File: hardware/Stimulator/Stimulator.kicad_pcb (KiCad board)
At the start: 2 copper layers, 49.5 x 33 mm, 52 parts, among them P1 CONN_3X2, P10 CONN_10X2, P12 CONN_8X2, P2 CONN_9X2, Q1 2N7002, Q2 2N7002, Q3 2N7002, Q4 2N7002, Q5 2N7002, Q6 2N7002, U1 MCP42010, U2 MCP42010, U3 MCP42010, U4 MCP42010

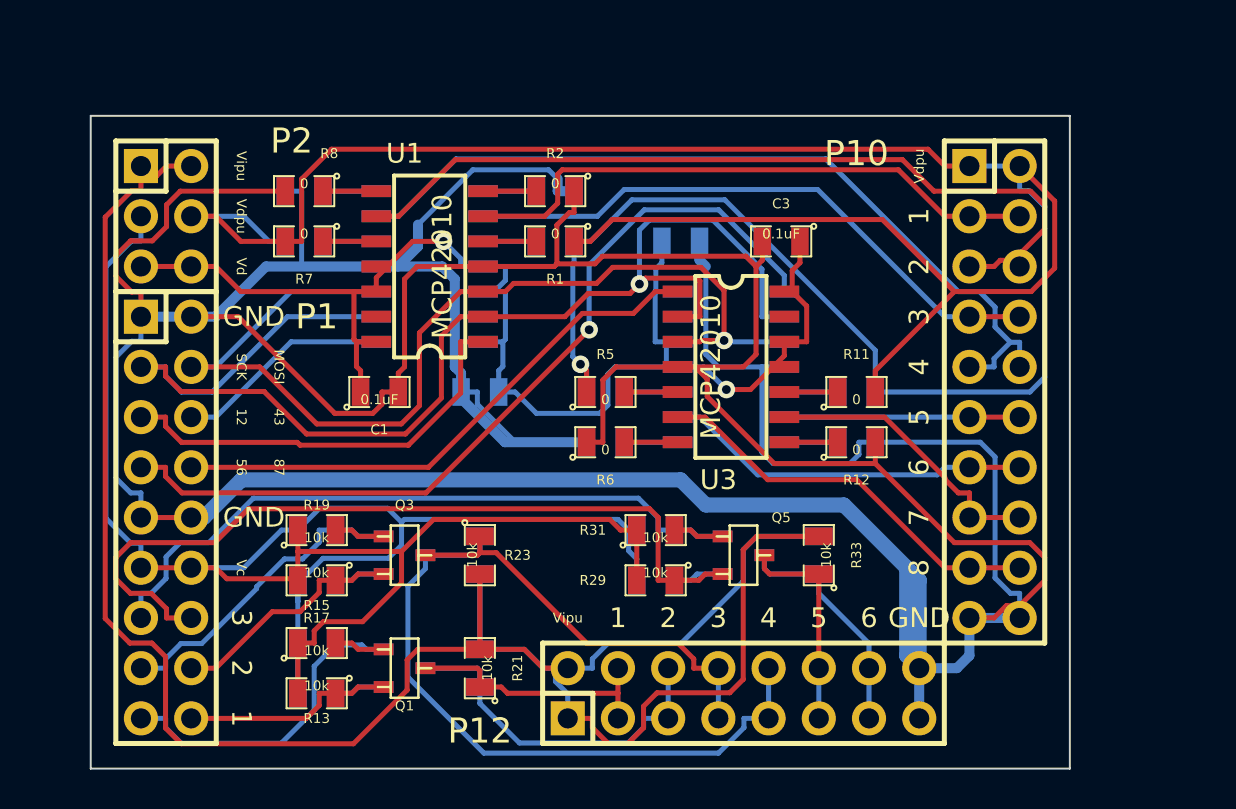
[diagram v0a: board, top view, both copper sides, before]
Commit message: 
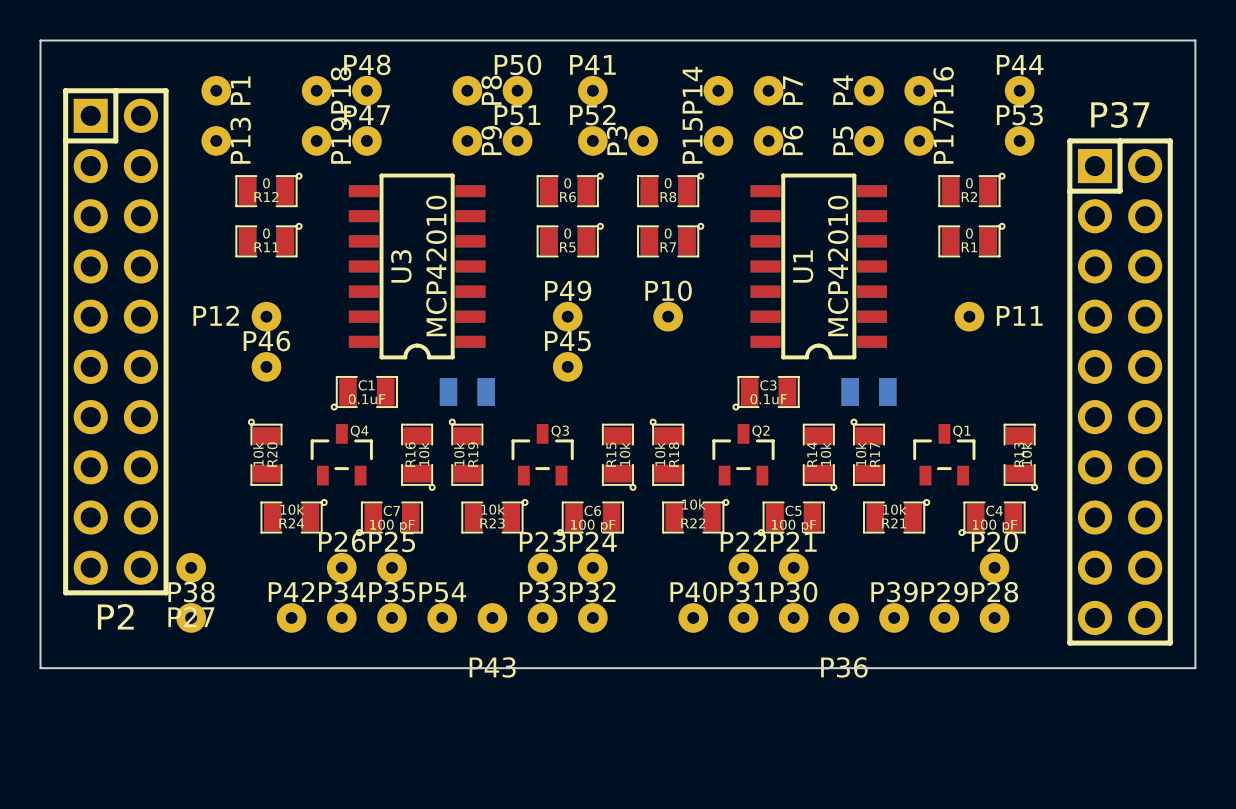
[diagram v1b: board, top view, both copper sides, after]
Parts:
- removed Q5, Q6: 2N7002, Transistors_SMD:sot23
- removed R29, R30, R31, R32, R33, R34: 10k, SMD_Packages:SM0805
- added C5: 100 pF, SMD_Packages:SM0805, F.Cu at (160.0, 82.5)
- added C6: 100 pF, SMD_Packages:SM0805, F.Cu at (149.9, 82.5)
- added C7: 100 pF, SMD_Packages:SM0805, F.Cu at (139.7, 82.5)
- added C8: 0.1uF, SMD_Packages:SM0805, B.Cu at (143.5, 76.2)
- added P11: CONN_1, Stimulator:1PIN, F.Cu at (168.9, 72.4)
- added P13: CONN_1, Stimulator:1PIN, F.Cu at (130.8, 63.5)
- added P14: CONN_1, Stimulator:1PIN, F.Cu at (156.2, 61.0)
- added P15: CONN_1, Stimulator:1PIN, F.Cu at (156.2, 63.5)
- added P16: CONN_1, Stimulator:1PIN, F.Cu at (166.4, 61.0)
- added P17: CONN_1, Stimulator:1PIN, F.Cu at (166.4, 63.5)
- added P18: CONN_1, Stimulator:1PIN, F.Cu at (135.9, 61.0)
- added P19: CONN_1, Stimulator:1PIN, F.Cu at (135.9, 63.5)
- added P20: CONN_1, Stimulator:1PIN, F.Cu at (170.2, 85.1)
- added P21: CONN_1, Stimulator:1PIN, F.Cu at (160.0, 85.1)
- added P22: CONN_1, Stimulator:1PIN, F.Cu at (157.5, 85.1)
- added P23: CONN_1, Stimulator:1PIN, F.Cu at (147.3, 85.1)
- added P24: CONN_1, Stimulator:1PIN, F.Cu at (149.9, 85.1)
- added P25: CONN_1, Stimulator:1PIN, F.Cu at (139.7, 85.1)
- added P26: CONN_1, Stimulator:1PIN, F.Cu at (137.2, 85.1)
- added P27: CONN_1, Stimulator:1PIN, F.Cu at (129.5, 85.1)
- added P28: CONN_1, Stimulator:1PIN, F.Cu at (170.2, 87.6)
- added P29: CONN_1, Stimulator:1PIN, F.Cu at (167.6, 87.6)
- added P3: CONN_1, Stimulator:1PIN, F.Cu at (152.4, 63.5)
- added P30: CONN_1, Stimulator:1PIN, F.Cu at (160.0, 87.6)
- added P31: CONN_1, Stimulator:1PIN, F.Cu at (157.5, 87.6)
- added P32: CONN_1, Stimulator:1PIN, F.Cu at (149.9, 87.6)
- added P33: CONN_1, Stimulator:1PIN, F.Cu at (147.3, 87.6)
- added P34: CONN_1, Stimulator:1PIN, F.Cu at (137.2, 87.6)
- added P35: CONN_1, Stimulator:1PIN, F.Cu at (139.7, 87.6)
- added P36: CONN_1, Stimulator:1PIN, F.Cu at (162.6, 87.6)
- added P37: CONN_10X2, Pin_Headers:Pin_Header_Straight_2x10, F.Cu at (176.5, 76.2)
- added P38: CONN_1, Stimulator:1PIN, F.Cu at (129.5, 87.6)
- added P39: CONN_1, Stimulator:1PIN, F.Cu at (165.1, 87.6)
- added P4: CONN_1, Stimulator:1PIN, F.Cu at (163.8, 61.0)
- added P40: CONN_1, Stimulator:1PIN, F.Cu at (154.9, 87.6)
- added P41: CONN_1, Stimulator:1PIN, F.Cu at (149.9, 61.0)
- added P42: CONN_1, Stimulator:1PIN, F.Cu at (134.6, 87.6)
- added P43: CONN_1, Stimulator:1PIN, F.Cu at (144.8, 87.6)
- added P44: CONN_1, Stimulator:1PIN, F.Cu at (171.4, 61.0)
- added P45: CONN_1, Stimulator:1PIN, F.Cu at (148.6, 74.9)
- added P46: CONN_1, Stimulator:1PIN, F.Cu at (133.3, 74.9)
- added P47: CONN_1, Stimulator:1PIN, F.Cu at (138.4, 63.5)
- added P48: CONN_1, Stimulator:1PIN, F.Cu at (138.4, 61.0)
- added P49: CONN_1, Stimulator:1PIN, F.Cu at (148.6, 72.4)
- added P5: CONN_1, Stimulator:1PIN, F.Cu at (163.8, 63.5)
- added P50: CONN_1, Stimulator:1PIN, F.Cu at (146.1, 61.0)
- added P51: CONN_1, Stimulator:1PIN, F.Cu at (146.1, 63.5)
- added P52: CONN_1, Stimulator:1PIN, F.Cu at (149.9, 63.5)
- added P53: CONN_1, Stimulator:1PIN, F.Cu at (171.4, 63.5)
- added P54: CONN_1, Stimulator:1PIN, F.Cu at (142.2, 87.6)
- added P6: CONN_1, Stimulator:1PIN, F.Cu at (158.8, 63.5)
- added P7: CONN_1, Stimulator:1PIN, F.Cu at (158.8, 61.0)
- added P8: CONN_1, Stimulator:1PIN, F.Cu at (143.5, 61.0)
- added P9: CONN_1, Stimulator:1PIN, F.Cu at (143.5, 63.5)
- C4: value 0.1uF -> 100 pF; moved to F.Cu
- P1: value CONN_3X2 -> CONN_1; footprint Pin_Headers:Pin_Header_Straight_2x03 -> Stimulator:1PIN
- P10: value CONN_10X2 -> CONN_1; footprint Pin_Headers:Pin_Header_Straight_2x10 -> Stimulator:1PIN
- P12: value CONN_8X2 -> CONN_1; footprint Pin_Headers:Pin_Header_Straight_2x08 -> Stimulator:1PIN
- P2: value CONN_9X2 -> CONN_10X2; footprint Pin_Headers:Pin_Header_Straight_2x09 -> Pin_Headers:Pin_Header_Straight_2x10
- Q2, Q4, R14, R16, R18, R20, R22, R24: moved to F.Cu
- moved R13 37.6 mm to (171.4, 79.4), turned to 90 degrees
- moved R12 32.4 mm to (133.3, 66.0), turned to 180 degrees
- moved R26 32.4 mm to (133.3, 66.0), turned to 0 degrees
- moved R11 30.8 mm to (133.3, 68.6), turned to 180 degrees
- moved R25 30.8 mm to (133.3, 68.6), turned to 0 degrees
- moved P12 30.7 mm to (133.3, 72.4)
- moved R17 29.5 mm to (163.8, 79.4), turned to 270 degrees
- moved Q1 29.4 mm to (167.6, 79.4), turned to 0 degrees
- moved R14 27.1 mm to (161.3, 79.4), turned to 90 degrees
- moved R21 22.3 mm to (165.1, 82.5), turned to 180 degrees
- moved R18 21.5 mm to (153.7, 79.4), turned to 270 degrees
- moved C4 21.1 mm to (170.2, 82.5)
- moved R1 21.0 mm to (168.9, 68.6)
- moved R10 21.0 mm to (168.9, 66.0)
- moved R2 21.0 mm to (168.9, 66.0)
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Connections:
- C4 pad 1: /Vd -> /EIN_1
- C4 pad 2: GND -> /IN_1
- P1 pad 1: /Vipu -> GND
- P10 pad 1: /Vdpu -> Net-(P10-Pad1)
- P12 pad 1: /Vipu -> Net-(P12-Pad1)
- P2 pad 10: GND -> Net-(P2-Pad10)
- P2 pad 11: /Vc -> Net-(P2-Pad11)
- P2 pad 12: /Vc -> Net-(P2-Pad12)
- P2 pad 13: /IN_6 -> Net-(P2-Pad13)
- P2 pad 14: /IN_5 -> Net-(P2-Pad14)
- P2 pad 15: /IN_4 -> Net-(P2-Pad15)
- P2 pad 16: /IN_3 -> Net-(P2-Pad16)
- P2 pad 17: /IN_2 -> Net-(P2-Pad17)
- P2 pad 18: /IN_1 -> Net-(P2-Pad18)
- P2 pad 2: GND -> Net-(P2-Pad2)
- P2 pad 3: /SCK -> Net-(P2-Pad3)
- P2 pad 4: /MOSI -> Net-(P2-Pad4)
- P2 pad 5: /CS_12 -> Net-(P2-Pad5)
- P2 pad 6: /CS_43 -> Net-(P2-Pad6)
- P2 pad 7: /CS_56 -> Net-(P2-Pad7)
- P2 pad 8: /CS_87 -> Net-(P2-Pad8)
- P2 pad 9: GND -> Net-(P2-Pad9)
- R1 pad 1: /Vdpu -> /Vdpu_14
- R11 pad 2: /Vdpu -> /Vdpu_58
- R21 pad 2: /Vipu -> /Vipu12
- R22 pad 2: /Vipu -> /Vipu12
- R23 pad 2: /Vipu -> /Vipu34
- R24 pad 2: /Vipu -> /Vipu34
- R25 pad 1: /Vdpu -> /Vdpu_58
- R27 pad 2: /Vdpu -> /Vdpu_58
- R3 pad 1: /Vdpu -> /Vdpu_14
- R5 pad 1: /Vdpu -> /Vdpu_58
- R7 pad 2: /Vdpu -> /Vdpu_14
- R9 pad 2: /Vdpu -> /Vdpu_14
- U1 pad 13: (no net) -> Net-(P10-Pad1)
- U2 pad 13: (no net) -> Net-(P11-Pad1)
- U2 pad 6: /OUT4 -> /OUT3
- U2 pad 9: /OUT3 -> /OUT4
- U3 pad 1: /CS_87 -> /CS_56
- U3 pad 13: (no net) -> Net-(P12-Pad1)
- U3 pad 6: /OUT8 -> /OUT5
- U3 pad 9: /OUT7 -> /OUT6
- U4 pad 1: /CS_56 -> /CS_78
- U4 pad 13: (no net) -> Net-(P49-Pad1)
- U4 pad 6: /OUT5 -> /OUT7
- U4 pad 9: /OUT6 -> /OUT8
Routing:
- net GND: track 281.5 -> 0.00 mm
- net /Vdpu: track 142.5 -> 0.00 mm, vias 1 -> 0
- net /Vipu: track 112.3 -> 0.00 mm
- net /Vc: track 103.0 -> 0.00 mm
- net /Vd: track 71.9 -> 0.00 mm, vias 2 -> 0
- net /SCK: track 66.0 -> 0.00 mm, vias 1 -> 0
- net /MOSI: track 53.0 -> 0.00 mm, vias 1 -> 0
- net /CS_56: track 43.4 -> 0.00 mm, vias 1 -> 0
- net /OUT4: track 42.3 -> 0.00 mm
- net /OUT2: track 42.2 -> 0.00 mm
- net /IN_5: track 41.2 -> 0.00 mm
- net /IN_6: track 34.5 -> 0.00 mm
- net /EIN_4: track 33.5 -> 0.00 mm
- net /OUT3: track 30.4 -> 0.00 mm
- net /OUT1: track 30.0 -> 0.00 mm
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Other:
- board size 49.5 x 33 mm -> 58.4 x 31.8 mm
- board text removed: "1"
- board text removed: "12"
- board text removed: "2"
- board text removed: "3"
- board text removed: "4"
- board text removed: "43"
- board text removed: "5"
- board text removed: "56"
- board text removed: "6"
- board text removed: "7"
- board text removed: "8"
- board text removed: "87"
- board text removed: "GND"
- board text removed: "MOSI"
- board text removed: "SCK"
- board text removed: "Vc"
- board text removed: "Vd"
- board text removed: "Vdpu"
- board text removed: "Vipu"

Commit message: 
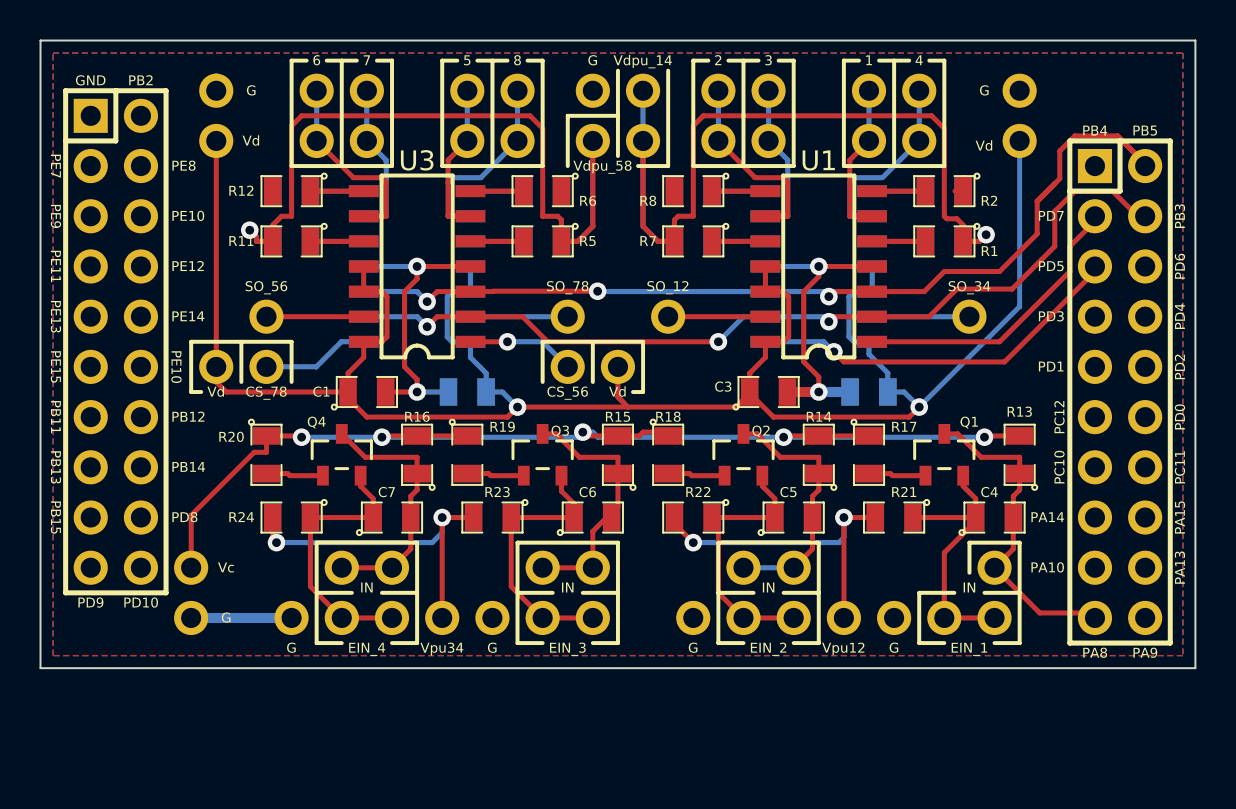
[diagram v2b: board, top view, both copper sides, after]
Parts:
- added P55: CONN_1, Stimulator:1PIN_A, F.Cu at (151.1, 74.9)
- added P56: CONN_1, Stimulator:1PIN_A, F.Cu at (130.8, 74.9)
- added P57: CONN_1, Stimulator:1PIN_A, F.Cu at (152.4, 61.0)
- P1, P10, P11, P12, P13, P14, P15, P16, P17, P18, P19, P20, P21, P22, P23, P24, P25, P26, P27, P28, P29, P3, P30, P31, P32, P33, P34, P35, P36, P38, P39, P4, P40, P41, P42, P43, P44, P45, P46, P47, P48, P49, P5, P50, P51, P52, P53, P54, P6, P7, P8, P9: footprint Stimulator:1PIN -> Stimulator:1PIN_A
- moved R1 1.27 mm to (167.6, 68.6)
- moved R10 1.27 mm to (167.6, 66.0)
- moved R11 1.27 mm to (134.6, 68.6)
- moved R12 1.27 mm to (134.6, 66.0)
- moved R2 1.27 mm to (167.6, 66.0)
- moved R25 1.27 mm to (134.6, 68.6)
- moved R26 1.27 mm to (134.6, 66.0)
- moved R27 1.27 mm to (147.3, 68.6)
- moved R28 1.27 mm to (147.3, 66.0)
- moved R3 1.27 mm to (154.9, 68.6)
- moved R4 1.27 mm to (154.9, 66.0)
- moved R5 1.27 mm to (147.3, 68.6)
- moved R6 1.27 mm to (147.3, 66.0)
- moved R7 1.27 mm to (154.9, 68.6)
- moved R8 1.27 mm to (154.9, 66.0)
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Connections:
- U2 pad 1: /CS_43 -> /CS_34
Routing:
- net /Vd: track 0.00 -> 109.2 mm, vias 0 -> 2
- net /Vc: track 0.00 -> 60.3 mm, vias 0 -> 5
- net /MOSI: track 0.00 -> 52.8 mm, vias 0 -> 3
- net /SCK: track 0.00 -> 45.7 mm, vias 0 -> 3
- net /Vdpu_14: track 0.00 -> 44.4 mm, vias 0 -> 1
- net /Vdpu_58: track 0.00 -> 42.3 mm, vias 0 -> 1
- net GND: track 0.00 -> 40.3 mm, vias 0 -> 4
- net /CS_34: track 0.00 -> 19.2 mm, vias 0 -> 1
- net /Vipu34: track 0.00 -> 17.5 mm, vias 0 -> 2
- net /Vipu12: track 0.00 -> 17.2 mm, vias 0 -> 2
- net /IN_1: track 0.00 -> 16.5 mm
- net /CS_12: track 0.00 -> 14.8 mm
- net /EIN_3: track 0.00 -> 14.2 mm
- net /EIN_1: track 0.00 -> 14.1 mm
- net /EIN_2: track 0.00 -> 14.0 mm
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- added copper zone on B.Cu, net GND
- added copper zone on F.Cu, net GND
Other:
- board text added: "1"
- board text added: "2"
- board text added: "3"
- board text added: "4"
- board text added: "5"
- board text added: "6"
- board text added: "7"
- board text added: "8"
- board text added: "CS_56"
- board text added: "CS_78"
- board text added: "EIN_1"
- board text added: "EIN_2"
- board text added: "EIN_3"
- board text added: "EIN_4"
- board text added: "G"
- board text added: "GND"
- board text added: "IN"
- board text added: "PA10"
- board text added: "PA13"
- board text added: "PA14"
- board text added: "PA15"
- board text added: "PA8"
- board text added: "PA9"
- board text added: "PB11"
- board text added: "PB12"
- board text added: "PB13"
- board text added: "PB14"
- board text added: "PB15"
- board text added: "PB2"
- board text added: "PB3"
- board text added: "PB4"
- board text added: "PB5"
- board text added: "PC10"
- board text added: "PC11"
- board text added: "PC12"
- board text added: "PD0"
- board text added: "PD1"
- board text added: "PD10"
- board text added: "PD2"
- board text added: "PD3"
- board text added: "PD4"
- board text added: "PD5"
- board text added: "PD6"
- board text added: "PD7"
- board text added: "PD8"
- board text added: "PD9"
- board text added: "PE10"
- board text added: "PE11"
- board text added: "PE12"
- board text added: "PE13"
- board text added: "PE14"
- board text added: "PE15"
- board text added: "PE7"
- board text added: "PE8"
- board text added: "PE9"
- board text added: "SO_12"
- board text added: "SO_34"
- board text added: "SO_56"
- board text added: "SO_78"
- board text added: "Vc"
- board text added: "Vd"
- board text added: "Vdpu_14"
- board text added: "Vdpu_58"
- board text added: "Vpu12"
- board text added: "Vpu34"

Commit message: 
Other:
- board text added: "DanMoto Stimulator June 2014"
